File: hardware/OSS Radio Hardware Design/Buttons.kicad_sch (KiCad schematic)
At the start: 44 parts

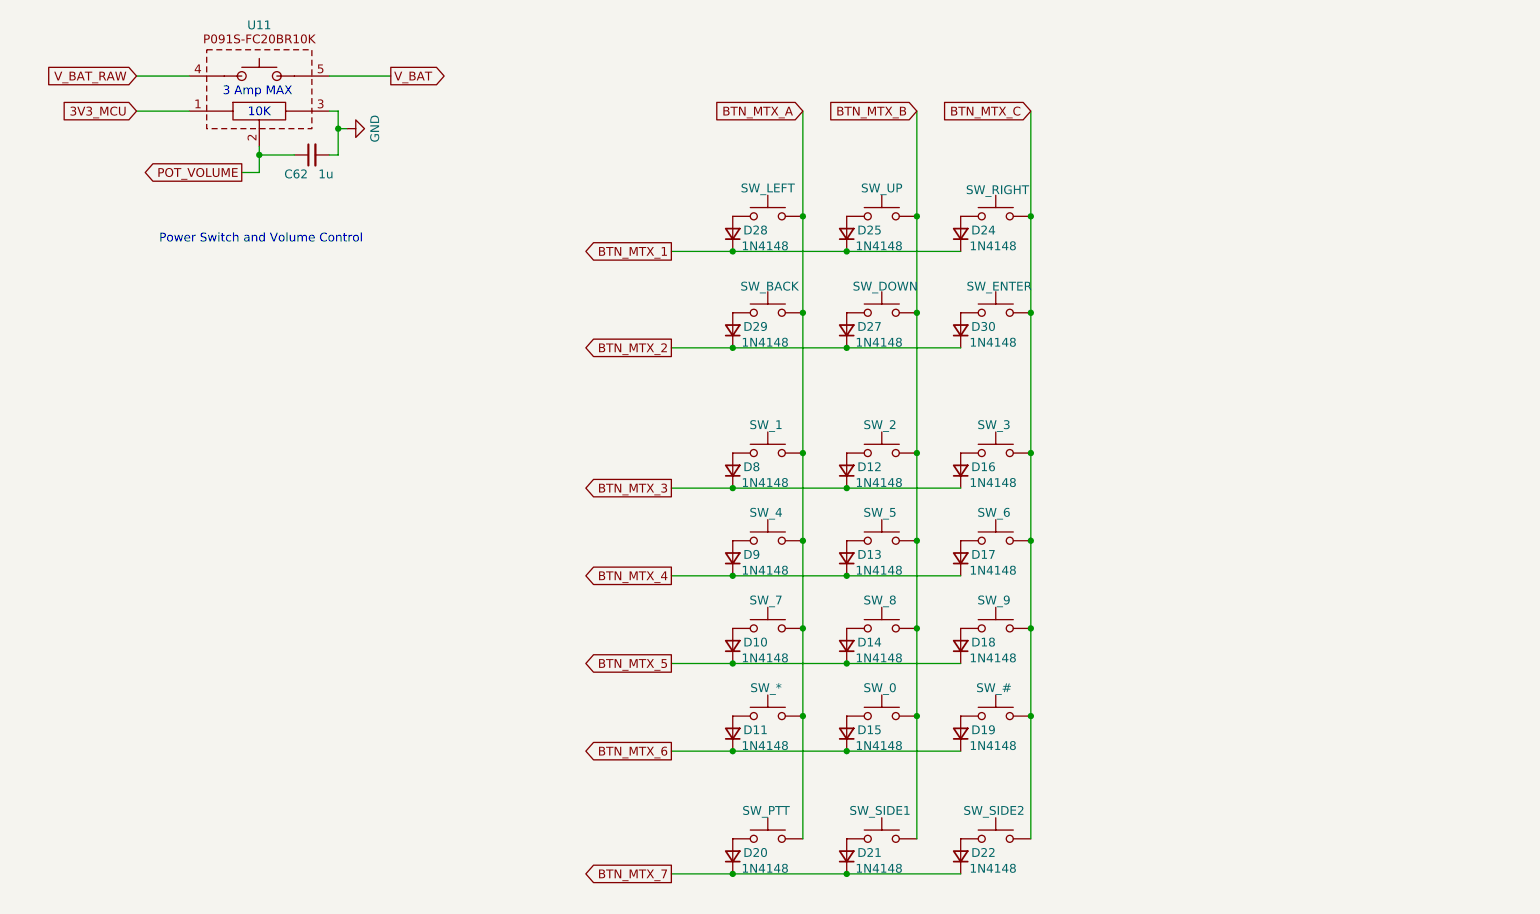
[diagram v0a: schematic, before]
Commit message: finished audio and encoder
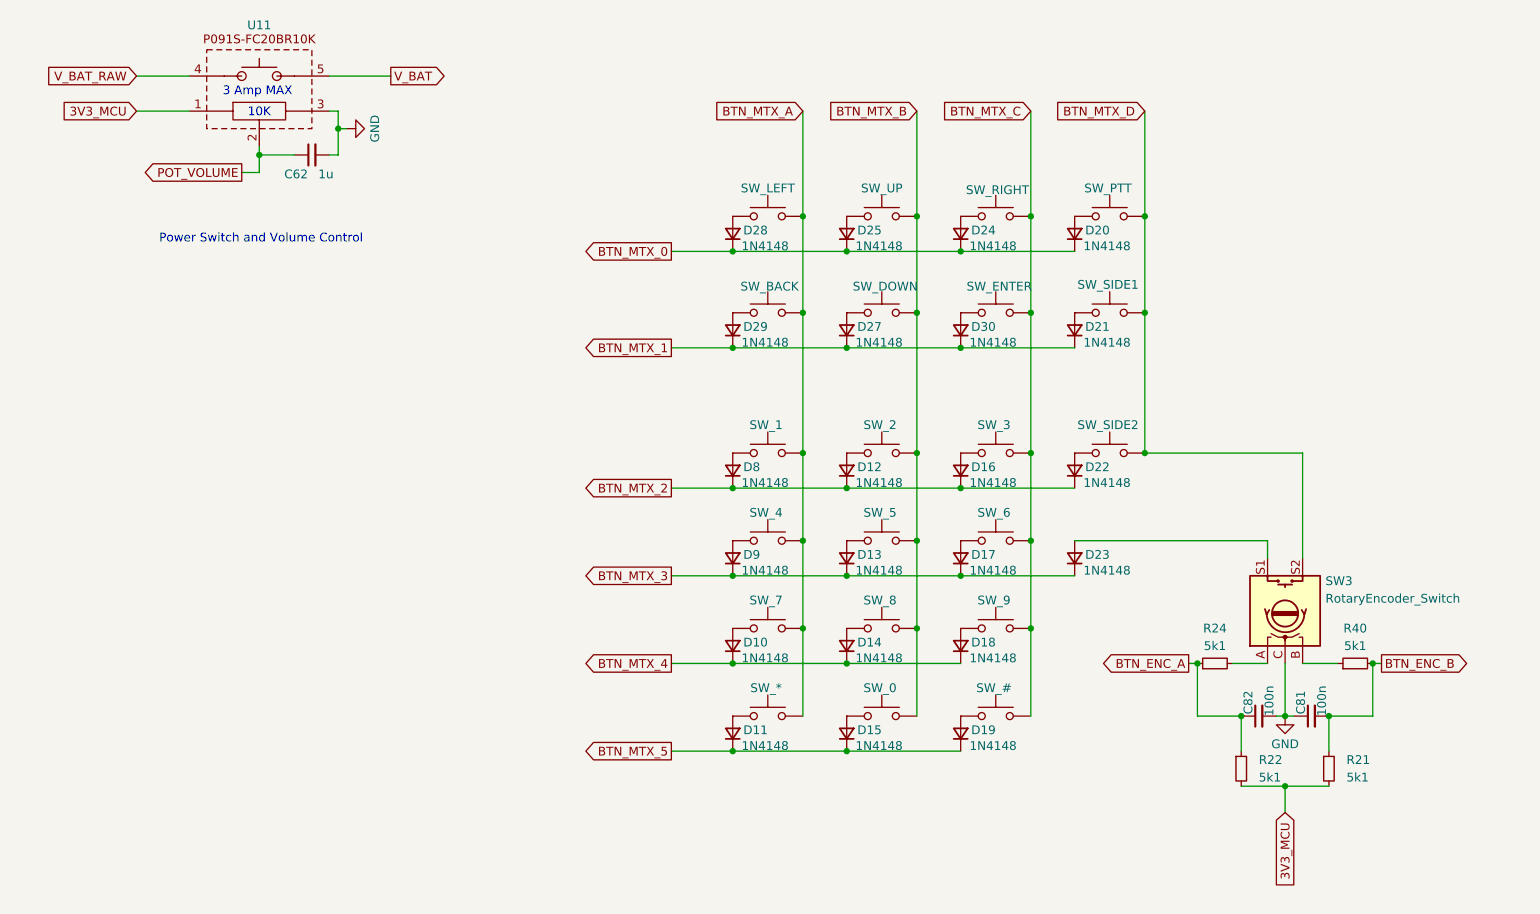
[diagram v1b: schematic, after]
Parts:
- added C81, C82: 100n, symbol Device:C_Small
- added D23: 1N4148, symbol Device:D_Small
- added R21, R22, R24, R40: 5k1, symbol Device:R_Small
- added SW3: RotaryEncoder_Switch, symbol Device:RotaryEncoder_Switch
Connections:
- net BTN_MTX_6 is gone; now on net BTN_MTX_5: D11.1 (K), D15.1 (K), D19.1 (K)
- net 3V3_MCU: now also R21.2, R22.2
- net BTN_MTX_1: now also D21.1 (K), D27.1 (K), D29.1 (K), D30.1 (K); no longer D24.1 (K), D25.1 (K), D28.1 (K)
- net BTN_MTX_2: now also D12.1 (K), D16.1 (K), D22.1 (K), D8.1 (K); no longer D27.1 (K), D29.1 (K), D30.1 (K)
- net BTN_MTX_3: now also D13.1 (K), D17.1 (K), D9.1 (K), D23.1 (K); no longer D12.1 (K), D16.1 (K), D8.1 (K)
- net BTN_MTX_4: now also D10.1 (K), D14.1 (K), D18.1 (K); no longer D13.1 (K), D17.1 (K), D9.1 (K)
- net BTN_MTX_5: no longer D10.1 (K), D14.1 (K), D18.1 (K)
- net BTN_MTX_A: no longer SW_PTT.2
- net BTN_MTX_B: no longer SW_SIDE1.2
- net BTN_MTX_C: no longer SW_SIDE2.2
- net GND: now also C81.1, C82.2, SW3.C
- removed net BTN_MTX_7: D20.1 (K), D21.1 (K), D22.1 (K)
- new net: R40.1, SW3.B
- new net: R24.2, SW3.A
- new net: D23.2 (A), SW3.S1
- new net BTN_ENC_A: C82.1, R22.1, R24.1
- new net BTN_ENC_B: C81.2, R21.1, R40.2
- new net BTN_MTX_0: D20.1 (K), D24.1 (K), D25.1 (K), D28.1 (K)
- new net BTN_MTX_D: SW3.S2, SW_PTT.2, SW_SIDE1.2, SW_SIDE2.2
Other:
- moved on the sheet: D20, D21, D22, SW_PTT, SW_SIDE1, SW_SIDE2

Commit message: added ESD diodes, MARS resistor, Charge LED, Status LED
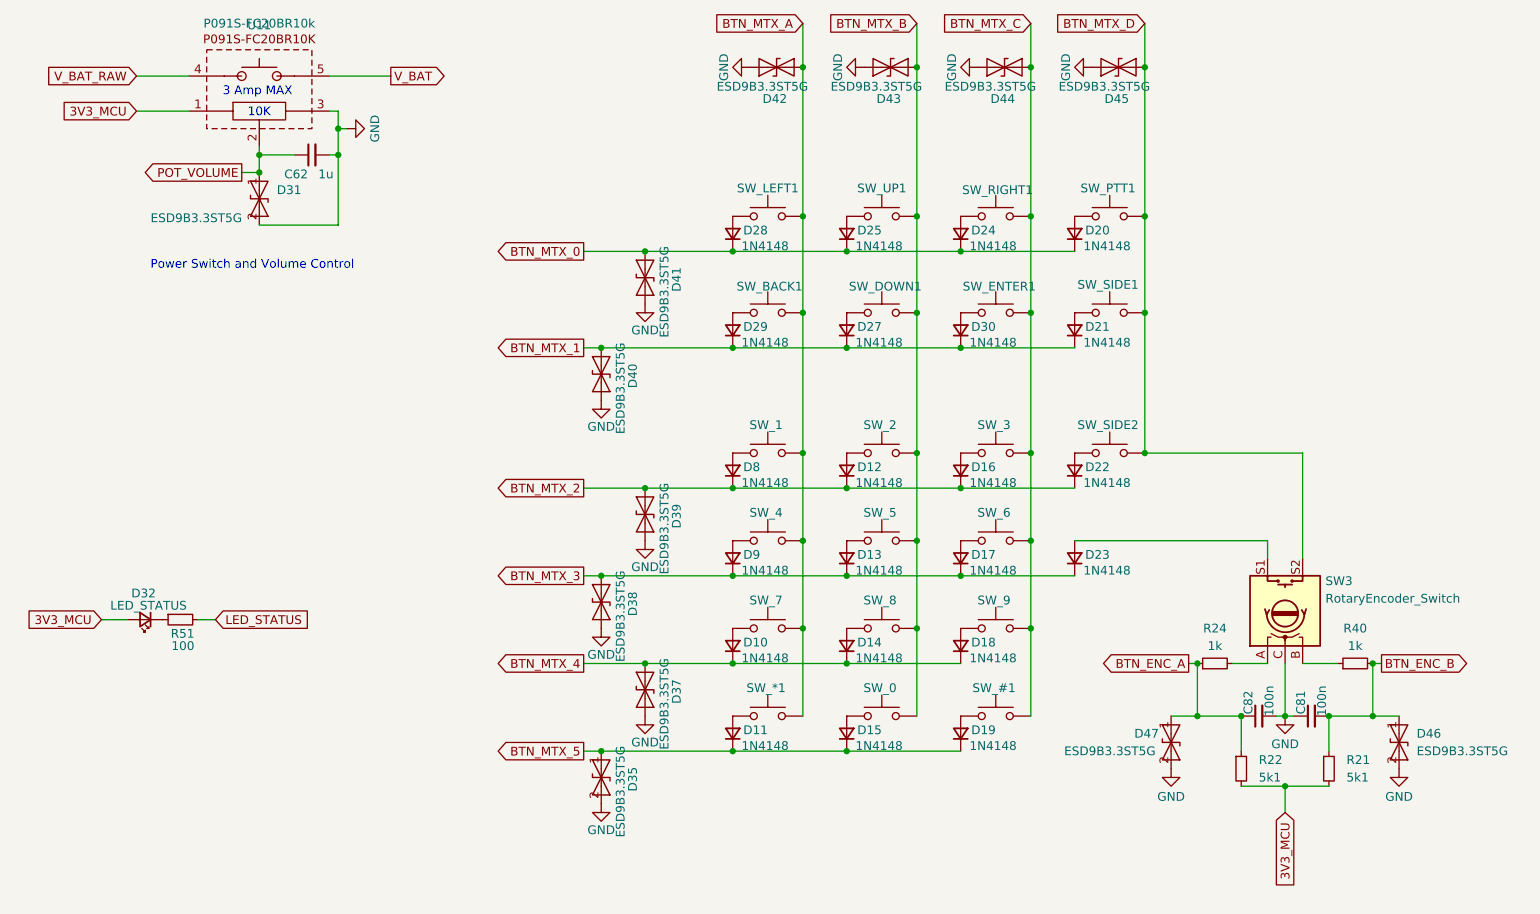
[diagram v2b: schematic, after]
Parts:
- added D31, D35, D37, D38, D39, D40, D41, D42, D43, D44, D45, D46, D47: ESD9B3.3ST5G, Diode_SMD:D_SOD-923, symbol Diode:ESD9B3.3ST5G
- added D32: LED_STATUS, symbol Device:LED_Small
- added R51: 100, symbol Device:R_Small
- R24, R40: value 5k1 -> 1k
- U11: value ~ -> P091S-FC20BR10k
- renumbered SW_# to SW_#1, SW_* to SW_*1, SW_BACK to SW_BACK1, SW_DOWN to SW_DOWN1, SW_ENTER to SW_ENTER1, SW_LEFT to SW_LEFT1, SW_PTT to SW_PTT1, SW_RIGHT to SW_RIGHT1, SW_UP to SW_UP1
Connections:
- net 3V3_MCU: now also D32.2 (A)
- net BTN_ENC_A: now also D47.1 (A1)
- net BTN_ENC_B: now also D46.1 (A1)
- net BTN_MTX_0: now also D41.1 (A1)
- net BTN_MTX_1: now also D40.1 (A1)
- net BTN_MTX_2: now also D39.1 (A1)
- net BTN_MTX_3: now also D38.1 (A1)
- net BTN_MTX_4: now also D37.1 (A1)
- net BTN_MTX_5: now also D35.1 (A1)
- net BTN_MTX_A: now also D42.1 (A1)
- net BTN_MTX_B: now also D43.1 (A1)
- net BTN_MTX_C: now also D44.1 (A1)
- net BTN_MTX_D: now also D45.1 (A1)
- net GND: now also D31.2 (A2), D35.2 (A2), D37.2 (A2), D38.2 (A2), D39.2 (A2), D40.2 (A2), D41.2 (A2), D42.2 (A2), D43.2 (A2), D44.2 (A2), D45.2 (A2), D46.2 (A2), D47.2 (A2)
- net POT_VOLUME: now also D31.1 (A1)
- new net: D32.1 (K), R51.1
- new net LED_STATUS: R51.2

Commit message: working on fooprints
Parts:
- C62: footprint (none) -> Capacitor_SMD:C_0603_1608Metric_Pad1.08x0.95mm_HandSolder
- C81, C82: footprint (none) -> Capacitor_SMD:C_0402_1005Metric_Pad0.74x0.62mm_HandSolder
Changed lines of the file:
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@@
 			)
 		)
-		(property "Footprint" ""
+		(property "Footprint" "Capacitor_SMD:C_0402_1005Metric_Pad0.74x0.62mm_HandSolder"
 			(at 207.01 134.62 0)
 			(effects
@@
 			)
 		)
-		(property "Footprint" ""
+		(property "Footprint" "Capacitor_SMD:C_0402_1005Metric_Pad0.74x0.62mm_HandSolder"
 			(at 199.39 134.62 0)
 			(effects
@@
 			)
 		)
-		(property "Footprint" ""
+		(property "Footprint" "Capacitor_SMD:C_0603_1608Metric_Pad1.08x0.95mm_HandSolder"
 			(at 62.23 53.34 0)
 			(effects
